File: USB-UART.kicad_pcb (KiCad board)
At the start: 4 copper layers, 66 x 16 mm, 46 parts, among them J1 USB_A, J2 Conn_01x06, J3 Conn_01x06, J4 Conn_01x06, U1 WE-TVS-82400152, U2 FT230XQ, U3 SN74LVC2T45DCUR, U4 SN74LVC2T45DCUR, U5 MAX232

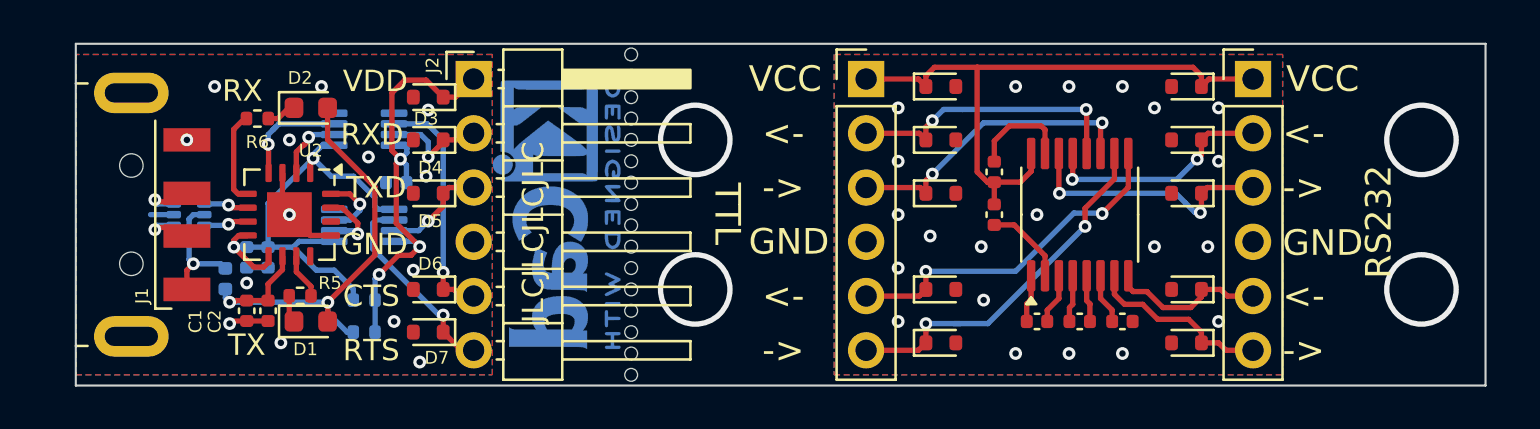
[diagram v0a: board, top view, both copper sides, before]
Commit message: change connector to USBC
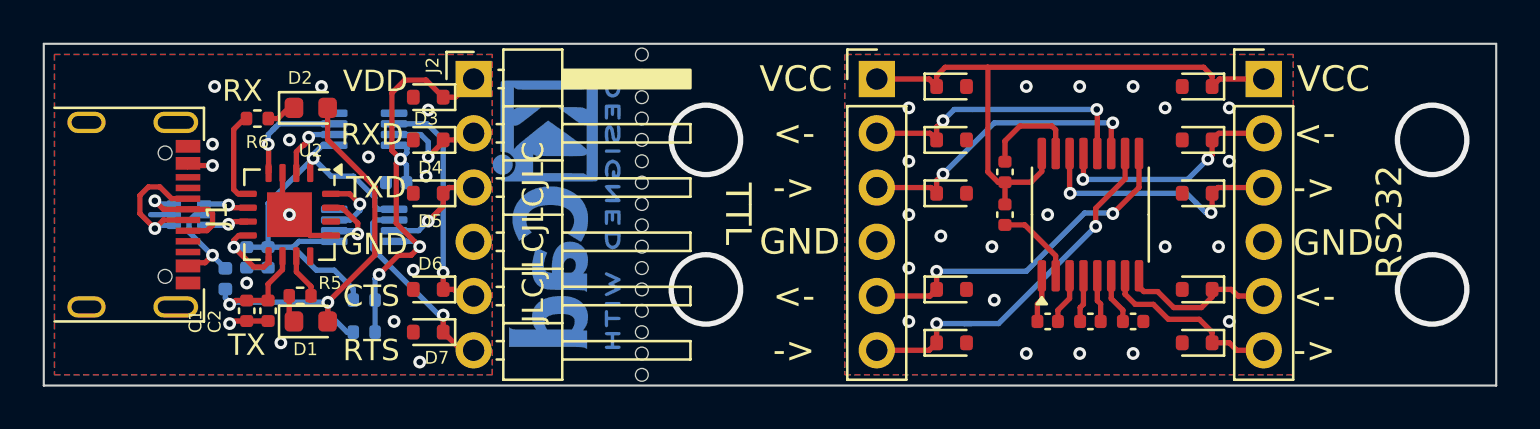
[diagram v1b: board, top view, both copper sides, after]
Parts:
- removed the REF** at (156.0, 94.5)
- removed the REF** at (156.0, 90.5)
- removed the REF** at (156.0, 102.5)
- removed the REF** at (156.0, 98.5)
- added REF**: mouse_bites 0.6mm, all_gk_fp_Ki8:mouse_bites 4x0.6mm, F.Cu at (156.5, 94.5)
- added REF**: mouse_bites 0.6mm, all_gk_fp_Ki8:mouse_bites 4x0.6mm, F.Cu at (156.5, 98.5)
- added REF**: mouse_bites 0.6mm, all_gk_fp_Ki8:mouse_bites 4x0.6mm, F.Cu at (156.5, 102.5)
- added REF**: mouse_bites 0.6mm, all_gk_fp_Ki8:mouse_bites 4x0.6mm, F.Cu at (156.5, 90.5)
- J1: value USB_A -> USB_C_Receptacle_USB2.0_16P; footprint Connector_USB_gk:USB3_A_Molex_480371000_Plug -> all_gk_fp_Ki8:USB_C_Receptacle_Wuerth_629722000214
- moved J1 5.30 mm to (131.0, 95.0), turned to -90 degrees
- moved C10 0.50 mm to (173.5, 93.0)
- moved C6 0.50 mm to (175.5, 100.0)
- moved C7 0.50 mm to (177.5, 100.0)
- moved C8 0.50 mm to (179.5, 100.0)
- moved C9 0.50 mm to (173.5, 95.0)
- moved D10 0.50 mm to (182.5, 94.0)
- moved D11 0.50 mm to (182.5, 98.5)
- moved D12 0.50 mm to (182.5, 101.0)
- moved D13 0.50 mm to (171.0, 89.0)
- moved D14 0.50 mm to (171.0, 91.5)
- moved D15 0.50 mm to (171.0, 94.0)
- moved D16 0.50 mm to (171.0, 98.5)
- moved D17 0.50 mm to (171.0, 101.0)
- moved D8 0.50 mm to (182.5, 89.0)
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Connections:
- U1 pad 1: Net-(J1-D-) -> Net-(J1-D--PadA7)
- U1 pad 3: Net-(J1-D+) -> Net-(J1-D+-PadA6)
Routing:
- net Net-(J1-D--PadA7): track 0.00 -> 7.34 mm, vias 0 -> 1
- net Net-(J1-D+-PadA6): track 0.00 -> 6.39 mm, vias 0 -> 1
- net VBUS: track 5.93 -> 10.4 mm, vias 1 -> 2
- net Net-(J1-D+): track 3.18 -> 0.00 mm, vias 1 -> 0
- net Net-(J1-D-): track 2.76 -> 0.00 mm, vias 1 -> 0
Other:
- board size 66 x 16 mm -> 68 x 16 mm
- board text added: "A"
